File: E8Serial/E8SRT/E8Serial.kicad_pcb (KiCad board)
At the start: 2 copper layers, 125 x 113 mm, 52 parts, among them J1 Conn_01x04_Male, J2 Conn_01x04_Male, J3 Conn_01x04_Male, J4 Conn_01x04_Male, Q1 BC548, Q2 BC548, Q3 BC548, SW1 NDB2, SW2 NDB1, SW3 PARITY ODD_EVEN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

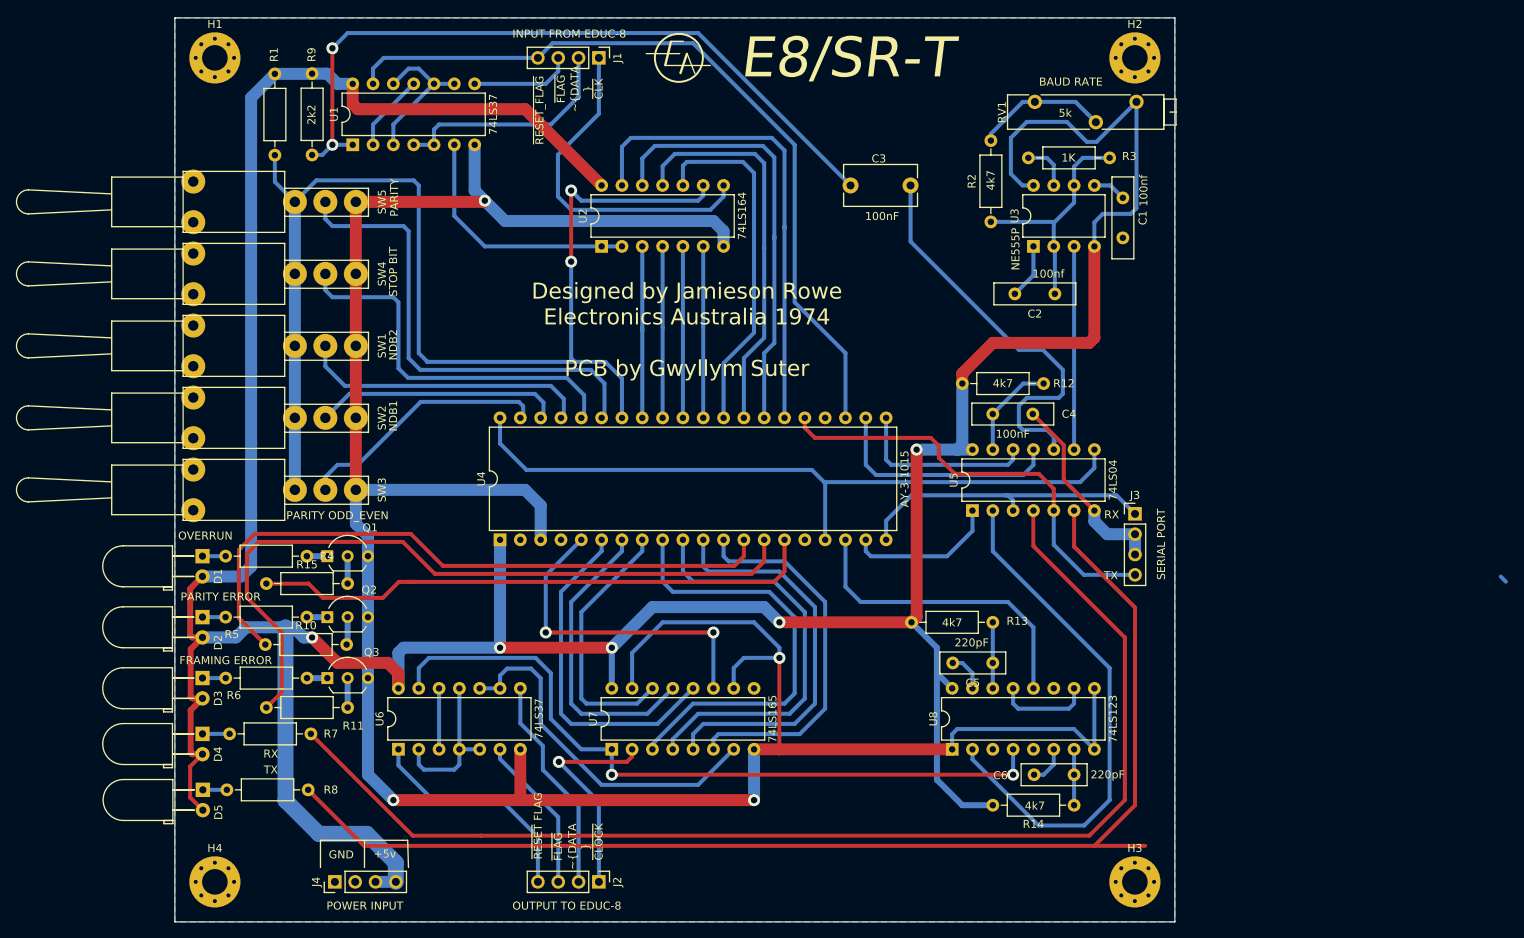
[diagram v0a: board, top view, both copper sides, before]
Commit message: Changes 20-7-2025 E8/T. Connected 3 missing supply rail tracks to ICS Added flood fill top and bottom to reduce noise E8/F Corrected labelling on RHS board to reflect EXT_LA not GND Changed fast slow switch operation so fast is in the DOWN position. E8/C. Ran a new track to the 2 pin JST connector from EXT_LA from 10 pin connector on SR input. Added files for E8MX, 2k byte memory expansion board
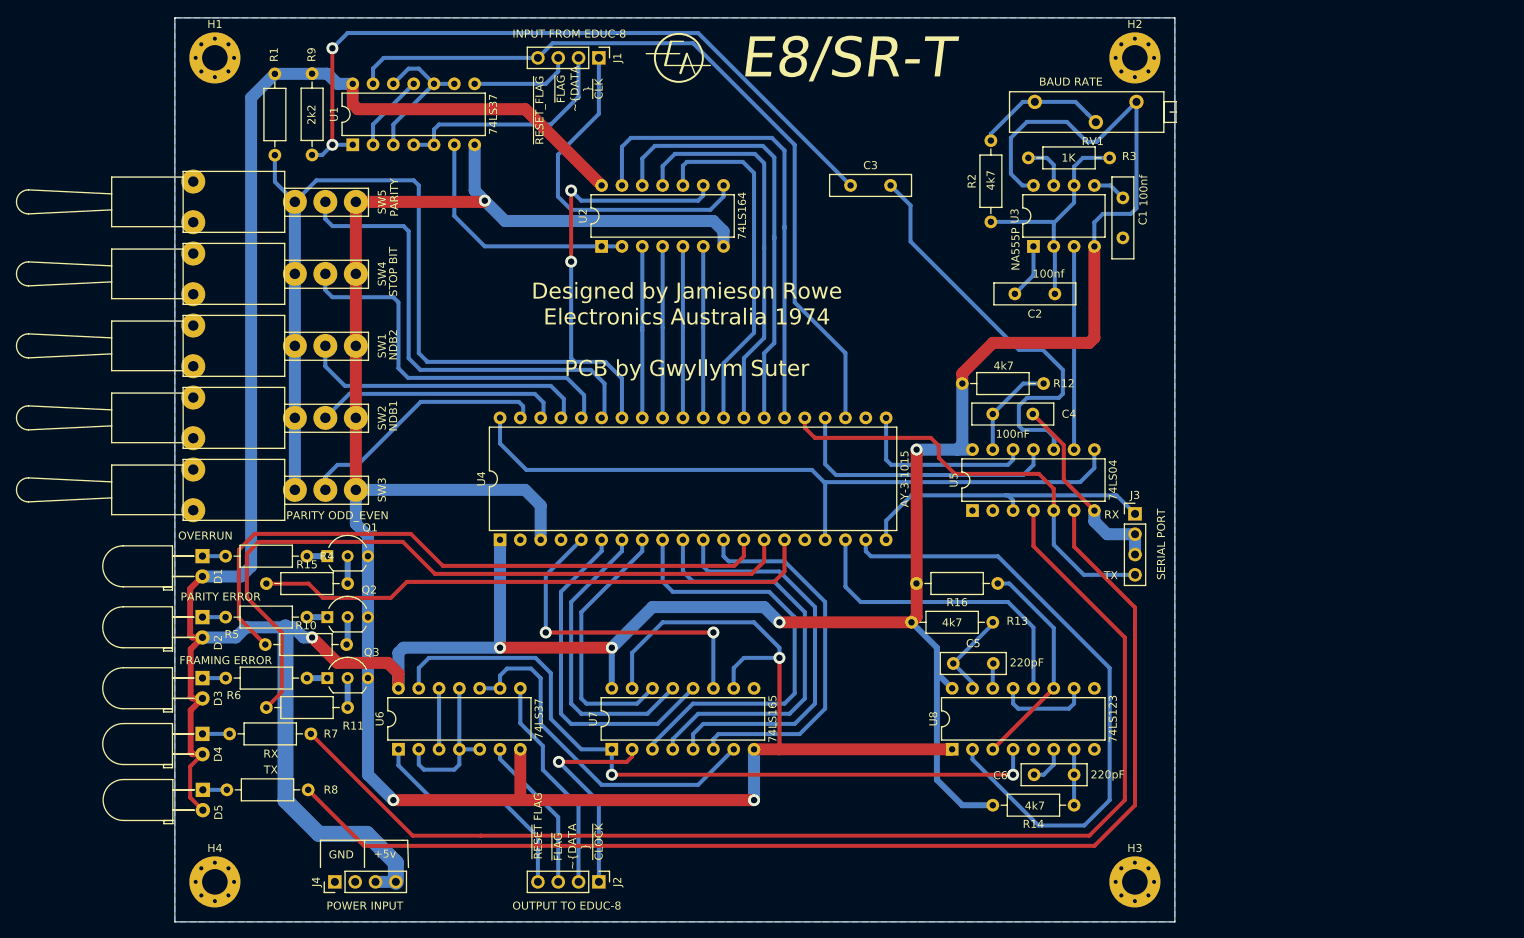
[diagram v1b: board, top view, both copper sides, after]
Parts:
- added R16: 4k7, Resistor_THT:R_Axial_DIN0207_L6.3mm_D2.5mm_P10.16mm_Horizontal, F.Cu at (142.9, 117.7)
- C3: footprint Capacitor_THT:C_Disc_D9.0mm_W5.0mm_P7.50mm -> Capacitor_THT:C_Disc_D10.0mm_W2.5mm_P5.00mm
- RV1: footprint Potentiometer_THT:Potentiometer_Bourns_3005_Horizontal -> Potentiometer_THT:Potentiometer_Bourns_3006P_Horizontal
- U3: value NE555P -> NA555P
- moved C5 4.94 mm to (137.3, 127.7), turned to 0 degrees
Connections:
- C5 pad 1: Net-(C5-Pad1) -> Net-(U8A-RCext)
- C5 pad 2: Net-(C5-Pad2) -> Net-(U8A-Cext)
- R13 pad 1: Net-(C5-Pad1) -> Net-(U8A-RCext)
- U4 pad 16: Net-(U4-Pad16) -> GND
- U4 pad 2: Net-(U4-Pad2) -> unconnected-(U4-N/C_(_+12V_ON_1013_)-Pad2)
- U4 pad 22: TBMT -> unconnected-(U4-TBMT-Pad22)
- U4 pad 24: Net-(U4-Pad24) -> TBMT
- U4 pad 4: Net-(U4-Pad4) -> GND
- U5 pad 1: ODA -> (no net)
- U5 pad 2: Net-(U5-Pad2) -> (no net)
- U7 pad 9: Net-(U7-Pad9) -> unconnected-(U7-Q7-Pad9)
- U8 pad 11: Net-(U8-Pad11) -> Net-(U8A-Clr)
- U8 pad 14: Net-(C5-Pad1) -> Net-(U8A-Cext)
- U8 pad 15: Net-(C5-Pad2) -> Net-(U8A-RCext)
- U8 pad 2: Net-(U5-Pad2) -> ODA
- U8 pad 3: Net-(U8-Pad3) -> Net-(U8A-Clr)
- U8 pad 5: Net-(U8-Pad5) -> unconnected-(U8B-Q-Pad5)
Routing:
- net Net-(U5-Pad2): track 65.4 -> 0.00 mm
- net ODA: track 18.9 -> 77.6 mm
- net GND: track 352.2 -> 323.6 mm
- net Net-(U8A-Clr): track 0.00 -> 27.6 mm
- net Net-(U8A-RCext): track 0.00 -> 11.3 mm
- net Net-(C5-Pad1): track 8.25 -> 0.00 mm
- net Net-(R8-Pad1): track 154.7 -> 148.4 mm
- net TBMT: track 29.8 -> 34.8 mm
- net Net-(C5-Pad2): track 4.89 -> 0.00 mm
- net Net-(U8A-Cext): track 0.00 -> 3.13 mm
- net Net-(C3-Pad2): track 51.0 -> 52.1 mm
- net OVERRUN: track 71.8 -> 70.8 mm
- net (no net): track 0.90 -> 0.00 mm
